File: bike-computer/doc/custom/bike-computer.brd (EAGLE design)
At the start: 100 x 80 mm, 3 parts

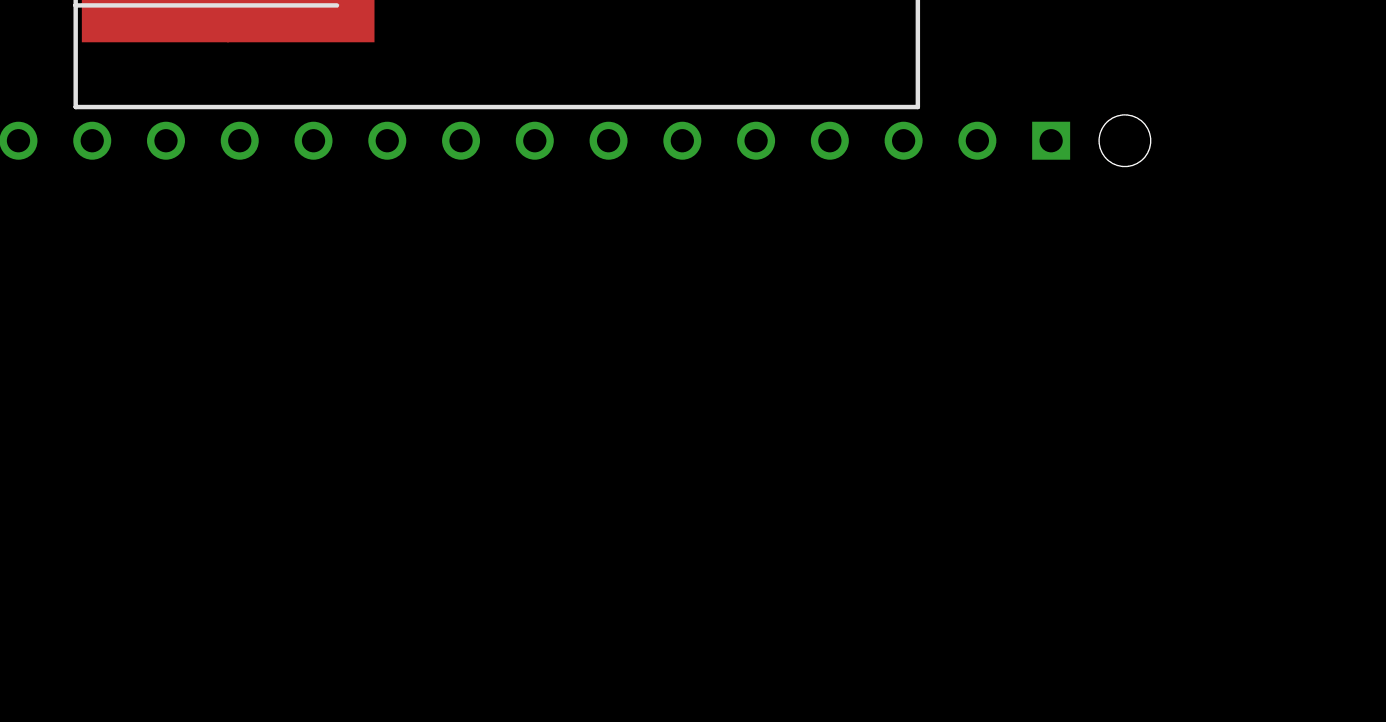
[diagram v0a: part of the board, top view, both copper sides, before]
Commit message: [Bike] Add a simple 0.9 inch OLED device. It fits to the hausing.
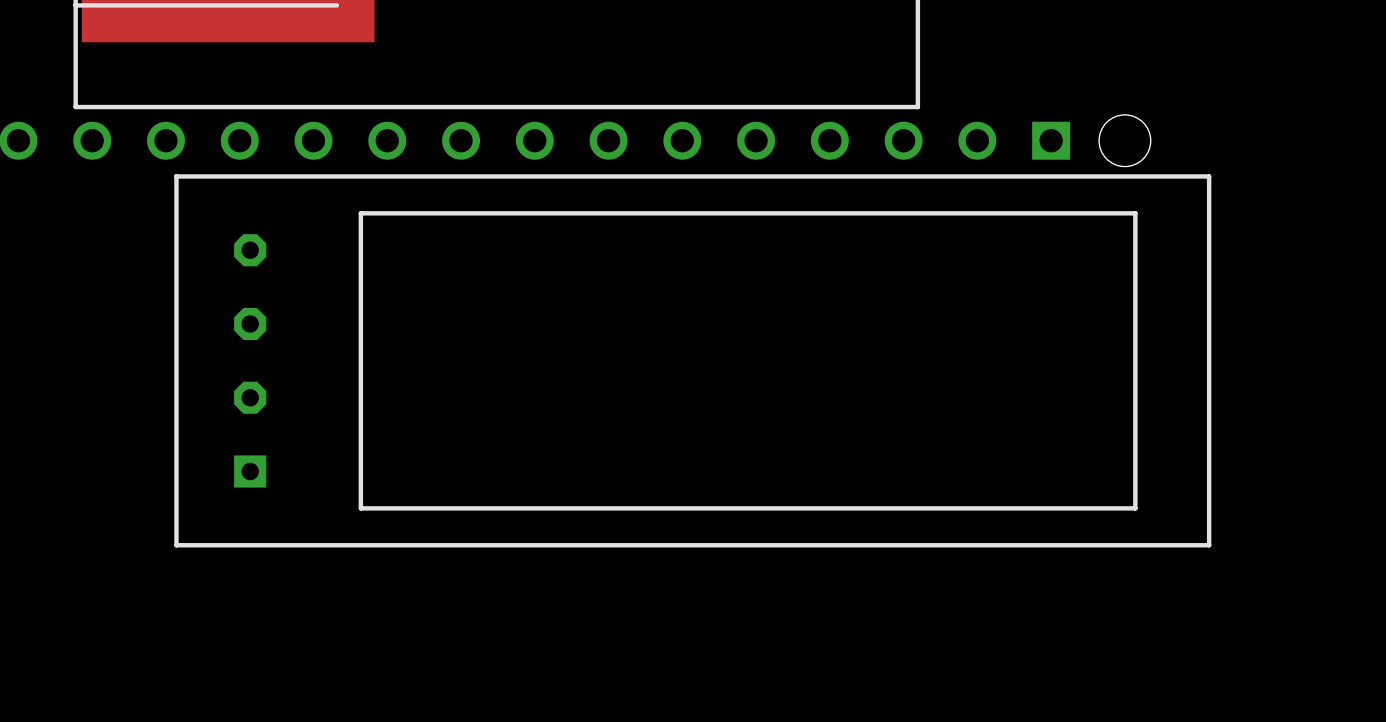
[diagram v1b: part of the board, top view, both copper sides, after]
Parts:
- added U$3: OLED_0.9, bike_computer:OLED_0.9
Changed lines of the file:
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@@
 <element name="U$1" library="bike_computer" package="STEPPER_GAUGE" value="STEPPER_GAUGE" x="44.05" y="46.85" smashed="yes"/>
 <element name="U$2" library="bike_computer" package="DRV8255_BOARD" value="DRV8825_BOARD" x="84.29" y="67.87" smashed="yes" rot="R90"/>
+<element name="U$3" library="bike_computer" package="OLED_0.9" value="OLED_0.9" x="50.8" y="22.86" smashed="yes"/>
 </elements>
 <signals>

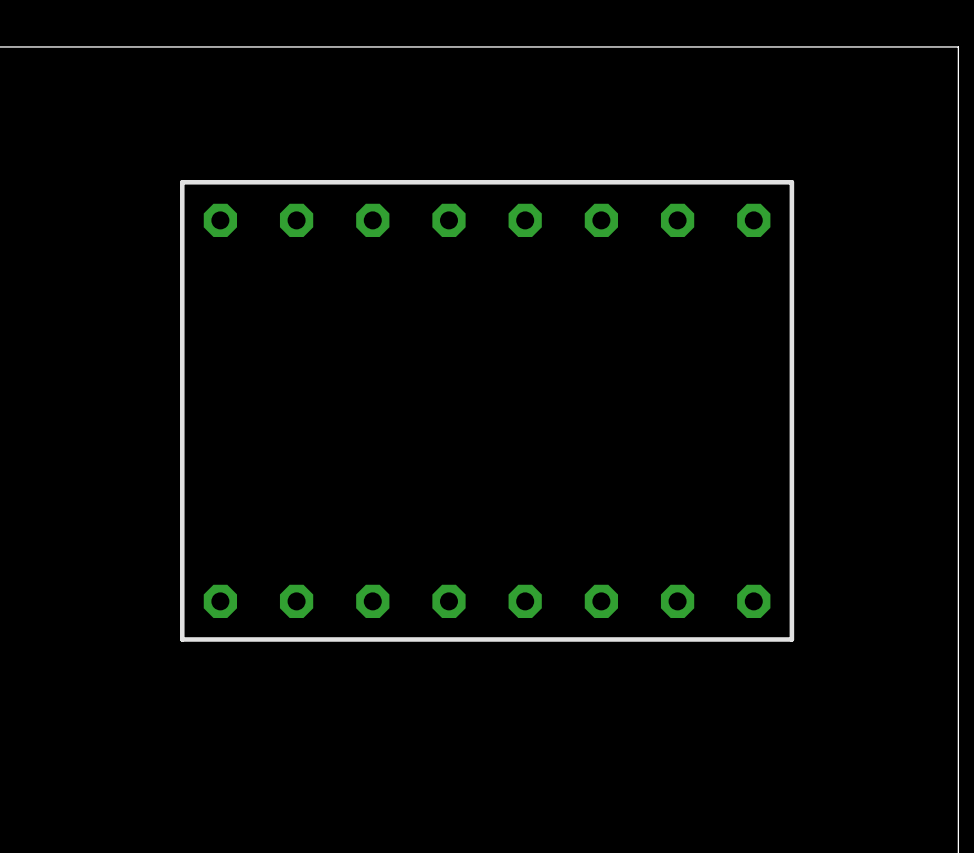
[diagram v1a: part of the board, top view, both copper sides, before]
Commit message: [Bike] Some changes for bike-computer
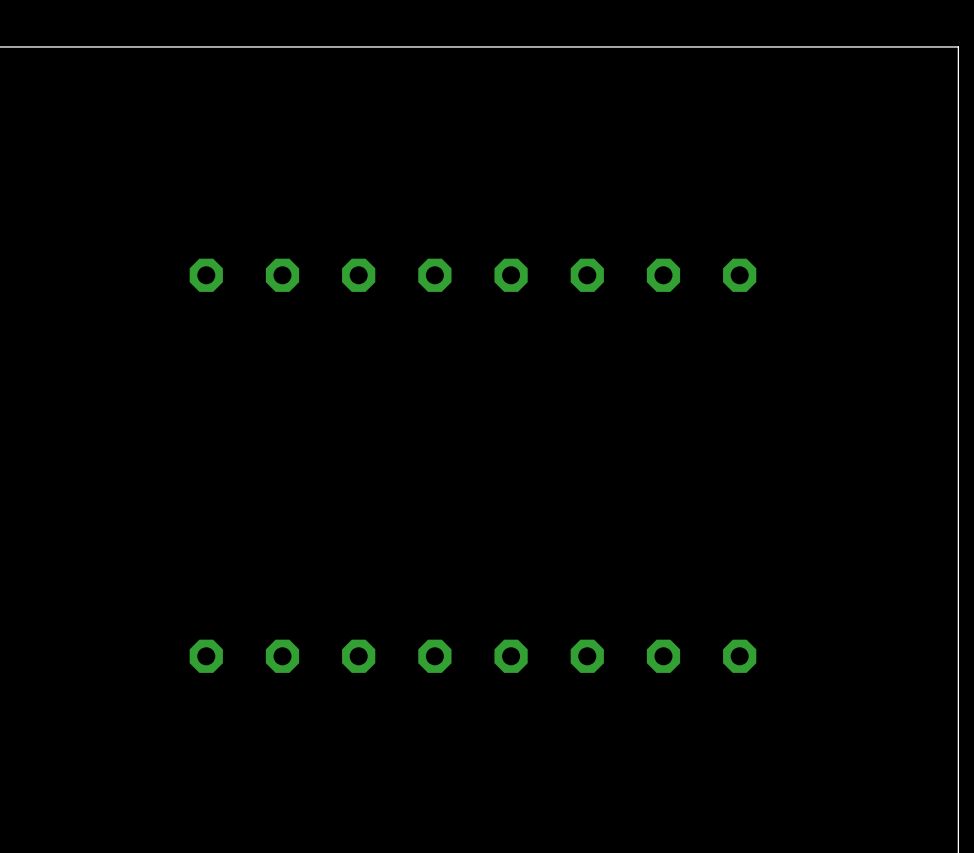
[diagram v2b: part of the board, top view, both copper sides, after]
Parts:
- removed U$2: DRV8825_BOARD, bike_computer:DRV8255_BOARD
- added DRV8825: DRV8825_BOARD, bike_computer:DRV8255_BOARD
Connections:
- new net SCL: ARDUINO_NANO1.9, U$3.SCL
- new net SDA: ARDUINO_NANO1.8, U$3.SDA
- net +12V: now also DRV8825.P$9; no longer U$2.P$9
- net +5V: now also DRV8825.P$5, DRV8825.P$6, U$3.VCC; no longer U$2.P$5, U$2.P$6
- net 0V: now also DRV8825.P$1, DRV8825.P$10, DRV8825.P$16, U$3.GND; no longer U$2.P$1, U$2.P$10, U$2.P$16
- net DIR: now also DRV8825.P$8; no longer U$2.P$8
- net N$1: now also DRV8825.P$11; no longer U$2.P$11
- net N$2: now also DRV8825.P$12; no longer U$2.P$12
- net N$3: now also DRV8825.P$13; no longer U$2.P$13
- net N$4: now also DRV8825.P$14; no longer U$2.P$14
- net STEP: now also DRV8825.P$7; no longer U$2.P$7
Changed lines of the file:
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@@
 </element>
 <element name="U$1" library="bike_computer" package="STEPPER_GAUGE" value="STEPPER_GAUGE" x="44.05" y="46.85" smashed="yes"/>
-<element name="U$2" library="bike_computer" package="DRV8255_BOARD" value="DRV8825_BOARD" x="84.29" y="67.87" smashed="yes" rot="R90"/>
 <element name="U$3" library="bike_computer" package="OLED_0.9" value="OLED_0.9" x="50.8" y="22.86" smashed="yes"/>
+<element name="DRV8825" library="bike_computer" package="DRV8255_BOARD" value="DRV8825_BOARD" x="83.82" y="66.04" smashed="yes" rot="MR90">
+<attribute name="NAME" x="91.44" y="62.23" size="1.778" layer="26" rot="MR90"/>
+</element>
 </elements>
 <signals>
@@
 </signal>
 <signal name="N$1">
-<contactref element="U$2" pad="P$11"/>
 <contactref element="U$1" pad="P$5"/>
 <contactref element="U$1" pad="P$6"/>
-<wire x1="45.8" y1="58.85" x2="80.48" y2="74.22" width="0" layer="19" extent="1-1"/>
+<contactref element="DRV8825" pad="P$11"/>
+<wire x1="45.8" y1="58.85" x2="87.63" y2="72.39" width="0" layer="19" extent="1-1"/>
 <wire x1="39.55" y1="58.85" x2="45.8" y2="58.85" width="0" layer="19" extent="1-1"/>
 </signal>
 <signal name="N$2">
-<contactref element="U$2" pad="P$12"/>
 <contactref element="U$1" pad="P$7"/>
 <contactref element="U$1" pad="P$8"/>
-<wire x1="46.55" y1="51.85" x2="83.02" y2="74.22" width="0" layer="19" extent="1-1"/>
+<contactref element="DRV8825" pad="P$12"/>
+<wire x1="46.55" y1="51.85" x2="85.09" y2="72.39" width="0" layer="19" extent="1-1"/>
 <wire x1="40.3" y1="51.85" x2="46.55" y2="51.85" width="0" layer="19" extent="1-1"/>
 </signal>
 <signal name="N$3">
-<contactref element="U$2" pad="P$13"/>
 <contactref element="U$1" pad="P$1"/>
 <contactref element="U$1" pad="P$2"/>
-<wire x1="37.3" y1="42.1" x2="85.56" y2="74.22" width="0" layer="19" extent="1-1"/>
+<contactref element="DRV8825" pad="P$13"/>
+<wire x1="37.3" y1="42.1" x2="82.55" y2="72.39" width="0" layer="19" extent="1-1"/>
 <wire x1="32.3" y1="42.1" x2="37.3" y2="42.1" width="0" layer="19" extent="1-1"/>
 </signal>
 <signal name="N$4">
-<contactref element="U$2" pad="P$14"/>
 <contactref element="U$1" pad="P$3"/>
 <contactref element="U$1" pad="P$4"/>
-<wire x1="37.3" y1="35.1" x2="88.1" y2="74.22" width="0" layer="19" extent="1-1"/>
+<contactref element="DRV8825" pad="P$14"/>
+<wire x1="37.3" y1="35.1" x2="80.01" y2="72.39" width="0" layer="19" extent="1-1"/>
 <wire x1="32.3" y1="35.1" x2="37.3" y2="35.1" width="0" layer="19" extent="1-1"/>
 </signal>
 <signal name="0V">
-<contactref element="U$2" pad="P$16"/>
-<contactref element="U$2" pad="P$10"/>
-<contactref element="U$2" pad="P$1"/>
 <contactref element="ARDUINO_NANO1" pad="14"/>
-<wire x1="75.4" y1="61.52" x2="77.94" y2="74.22" width="0" layer="19" extent="1-1"/>
-<wire x1="93.18" y1="74.22" x2="77.94" y2="74.22" width="0" layer="19" extent="1-1"/>
-<wire x1="30.12" y1="30.44" x2="75.4" y2="61.52" width="0" layer="19" extent="1-1"/>
+<contactref element="U$3" pad="GND"/>
+<contactref element="DRV8825" pad="P$10"/>
+<contactref element="DRV8825" pad="P$16"/>
+<contactref element="DRV8825" pad="P$1"/>
+<wire x1="92.71" y1="59.69" x2="90.17" y2="72.39" width="0" layer="19" extent="1-1"/>
+<wire x1="74.93" y1="72.39" x2="90.17" y2="72.39" width="0" layer="19" extent="1-1"/>
+<wire x1="30.12" y1="30.44" x2="74.93" y2="72.39" width="0" layer="19" extent="1-1"/>
+<wire x1="35.56" y1="19.05" x2="30.12" y2="30.44" width="0" layer="19" extent="1-1"/>
+</signal>
+<signal name="+5V">
+<contactref element="ARDUINO_NANO1" pad="12"/>
+<contactref element="U$3" pad="VCC"/>
+<contactref element="DRV8825" pad="P$5"/>
+<contactref element="DRV8825" pad="P$6"/>
+<wire x1="80.01" y1="59.69" x2="82.55" y2="59.69" width="0" layer="19" extent="1-1"/>
+<wire x1="35.2" y1="30.44" x2="80.01" y2="59.69" width="0" layer="19" extent="1-1"/>
+<wire x1="35.56" y1="21.59" x2="35.2" y2="30.44" width="0" layer="19" extent="1-1"/>
+</signal>
+<signal name="STEP">
+<contactref element="ARDUINO_NANO1" pad="20"/>
+<contactref element="DRV8825" pad="P$7"/>
+<wire x1="37.74" y1="45.68" x2="77.47" y2="59.69" width="0" layer="19" extent="1-1"/>
+</signal>
+<signal name="DIR">
+<contactref element="ARDUINO_NANO1" pad="21"/>
+<contactref element="DRV8825" pad="P$8"/>
+<wire x1="40.28" y1="45.68" x2="74.93" y2="59.69" width="0" layer="19" extent="1-1"/>
+</signal>
+<signal name="SDA">
+<contactref element="U$3" pad="SDA"/>
+<contactref element="ARDUINO_NANO1" pad="8"/>
+<wire x1="35.56" y1="26.67" x2="45.36" y2="30.44" width="0" layer="19" extent="1-1"/>
+</signal>
+<signal name="SCL">
+<contactref element="U$3" pad="SCL"/>
+<contactref element="ARDUINO_NANO1" pad="9"/>
+<wire x1="35.56" y1="24.13" x2="42.82" y2="30.44" width="0" layer="19" extent="1-1"/>
 </signal>
 <signal name="+12V">
-<contactref element="U$2" pad="P$9"/>
-</signal>
-<signal name="+5V">
-<contactref element="U$2" pad="P$6"/>
-<contactref element="U$2" pad="P$5"/>
-<contactref element="ARDUINO_NANO1" pad="12"/>
-<wire x1="88.1" y1="61.52" x2="85.56" y2="61.52" width="0" layer="19" extent="1-1"/>
-<wire x1="35.2" y1="30.44" x2="88.1" y2="61.52" width="0" layer="19" extent="1-1"/>
-</signal>
-<signal name="STEP">
-<contactref element="U$2" pad="P$7"/>
-<contactref element="ARDUINO_NANO1" pad="20"/>
-<wire x1="37.74" y1="45.68" x2="90.64" y2="61.52" width="0" layer="19" extent="1-1"/>
-</signal>
-<signal name="DIR">
-<contactref element="U$2" pad="P$8"/>
-<contactref element="ARDUINO_NANO1" pad="21"/>
-<wire x1="40.28" y1="45.68" x2="93.18" y2="61.52" width="0" layer="19" extent="1-1"/>
+<contactref element="DRV8825" pad="P$9"/>
 </signal>
 </signals>

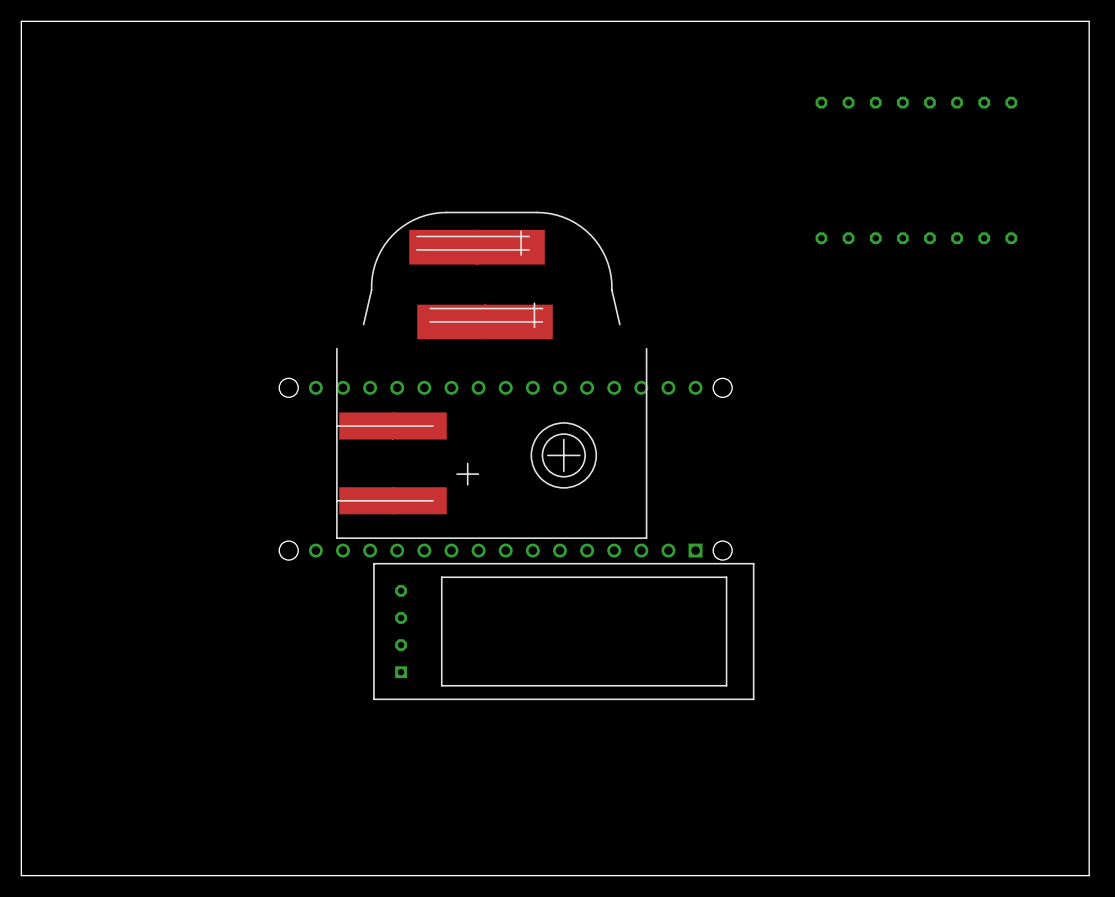
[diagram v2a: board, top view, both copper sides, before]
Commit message: [Bike] Further work on schematics.
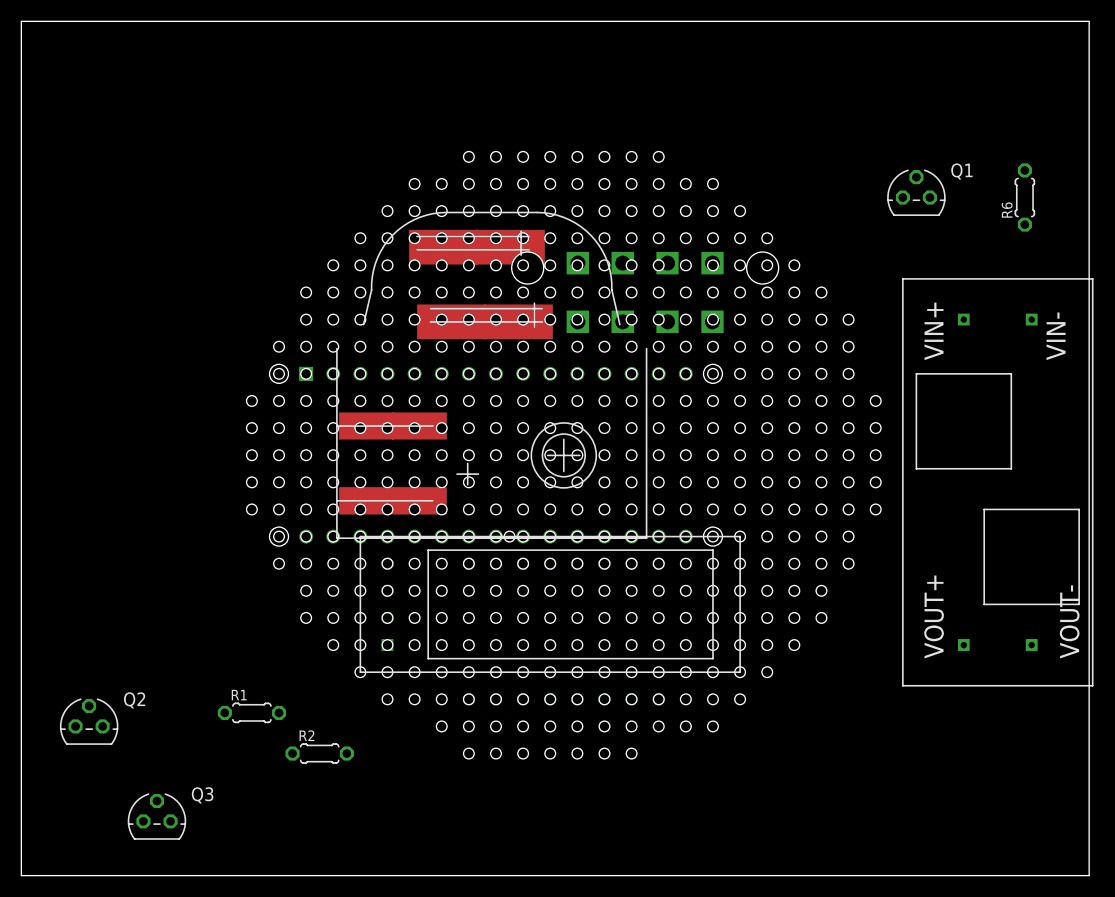
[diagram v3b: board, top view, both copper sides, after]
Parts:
- added Q1, Q2, Q3: 2N3820, transistor-small-signal:TO92F
- added R1, R2, R6: (no value), rcl:0204/5
- added U$2: STEP_UP_REG, bike_computer:STEP_UP_REG
- added X1: 5566-8, con-molex:5566-8
- moved DRV8825 54.4 mm to (50.8, 22.9)
- moved ARDUINO_NANO1 4.37 mm to (47.0, 39.4), turned to 180 degrees
- moved U$3 2.84 mm to (49.5, 25.4)
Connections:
- new net 12V_ENABLE: ARDUINO_NANO1.23, R6.1
- new net BACK_LIGHT_PWM: ARDUINO_NANO1.26, R2.1
- new net BACK_LIGHT_VOLTAGE: Q3.D, X1.3
- new net FRONT_LIGHT_PWM: ARDUINO_NANO1.25, R1.1
- new net FRONT_LIGHT_VOLTAGE: Q2.D, X1.6
- new net N$5: Q2.G, R1.2
- new net N$6: Q1.G, R6.2
- new net N$7: Q1.D, U$2.VIN+
- new net N$8: Q3.G, R2.2
- new net SPEED_INPUT: ARDUINO_NANO1.24, X1.5
- net +12V: now also U$2.VOUT+
- net +5V: now also Q1.S, Q2.S, Q3.S, X1.2
- net 0V: now also U$2.VIN-, U$2.VOUT-, X1.1
